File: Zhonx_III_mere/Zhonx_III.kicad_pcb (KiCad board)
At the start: 2 copper layers, 70 x 97 mm, 133 parts, among them K1 L_Motor, K2 R_Motor, K3 USART, P1 JTAG, Q1 FDV301N, Q2 FDV301N, U1 MCP73213, U10 BSL214N, U11 BSL214N, U12 24LC64T, U14 STM32F405RGT6, U16 Line_1, U17 Line_2, U18 Line_3, U19 Line_4, U2 A3918, U20 Line_5, U3 A3918, U4 LTC2955CTS8-2, U5 SIB911DK, U6 SI1551DL, U7 LM2940, U8 MCP1700, U9 MCP1700, X1 16MHz

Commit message: Update Base_V2 (CamBam DXF)
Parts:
- ADXR1, C103, C104, C17, C18, C19, C2, C20, C21, C22, C23, C24, C25, C27, C29, C30, C35, C36, C37, C38, C39, C40, C41, C43, D1, D11, D12, IR1, IR2, IR3, IR4, K1, K2, K3, L2, PL1, R1, R17, R18, R19, R22, R23, R3, R30, R34, R35, R38, R39, R44, R45, R48, R49, R50, R51, R52, SP1, U10, U11, U14, X1: moved to B.Cu
- C1, C10, C100, C101, C11, C12, C13, C14, C15, C16, C26, C28, C3, C31, C32, C33, C34, C4, C42, C44, C45, C5, C6, C7, C8, C9, P1, Q1, Q2, R10, R11, R12, R13, R14, R15, R16, R2, R20, R21, R24, R25, R26, R27, R28, R29, R31, R32, R33, R4, R5, R58, R6, R64, R67, R7, R8, R9, SCH1, U1, U12, U16, U17, U18, U19, U2, U20, U3, U4, U5, U6, U7, U8, U9: moved to F.Cu
- moved Q1 87.4 mm to (154.2, 125.6), turned to 180 degrees
- moved R8 86.5 mm to (153.7, 128.2), turned to 0 degrees
- moved C2 83.9 mm to (152.3, 129.2)
- moved C19 81.8 mm to (151.2, 129.2)
- moved R10 80.9 mm to (150.7, 129.7)
- moved IR1 79.1 mm to (149.7, 117.8), turned to 174 degrees
- moved R34 79.0 mm to (149.7, 128.8)
- moved C33 78.8 mm to (149.5, 129.7)
- moved R44 78.4 mm to (149.3, 120.9), turned to 0 degrees
- moved R35 77.4 mm to (148.8, 126.0), turned to 0 degrees
- moved D11 76.5 mm to (148.3, 186.0)
- moved R1 76.5 mm to (148.3, 183.5)
- moved R45 75.4 mm to (147.7, 120.9), turned to 0 degrees
- moved U10 73.4 mm to (146.6, 128.7)
- moved R18 72.5 mm to (146.0, 126.7), turned to 0 degrees
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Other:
- outline, holes or cut-outs redrawn

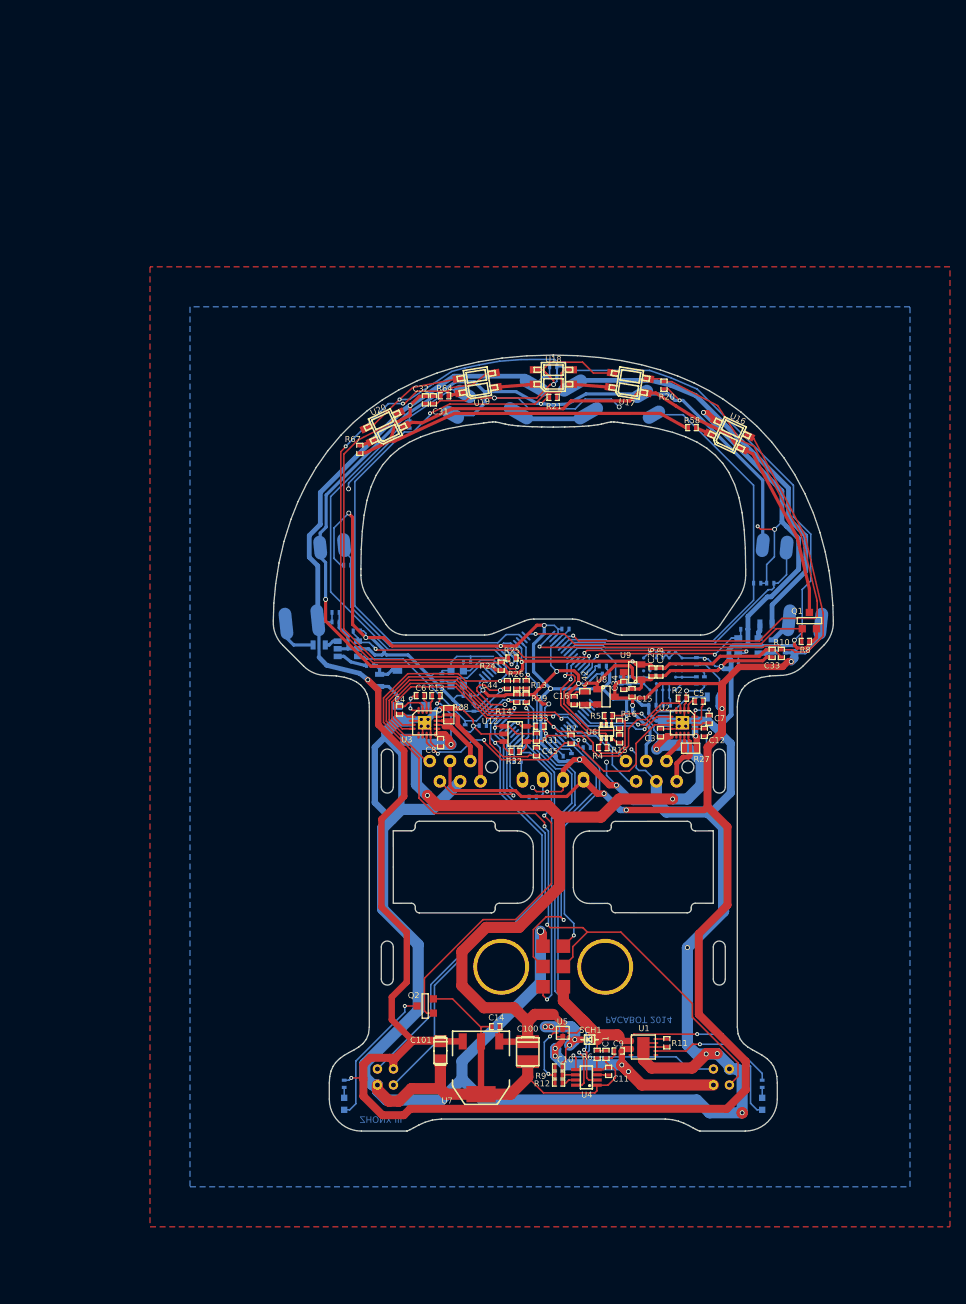
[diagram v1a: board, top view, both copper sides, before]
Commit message: repair mod librairies
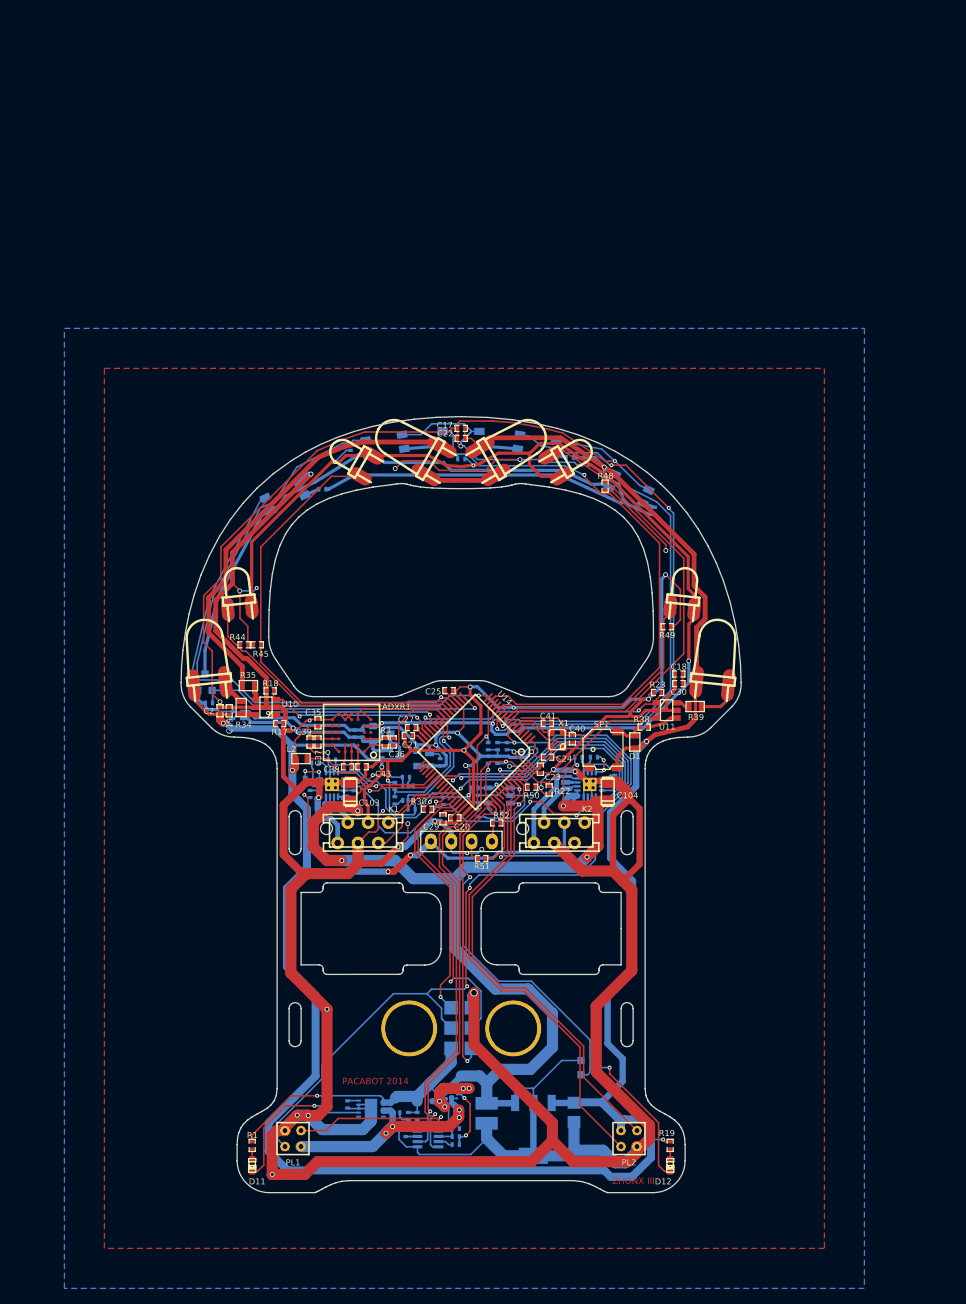
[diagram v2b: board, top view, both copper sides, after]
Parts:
- ADXR1, C103, C104, C17, C18, C19, C2, C20, C21, C22, C23, C24, C25, C27, C29, C30, C35, C36, C37, C38, C39, C40, C41, C43, D1, D11, D12, IR1, IR2, IR3, IR4, K1, K2, K3, L2, PL1, R1, R17, R18, R19, R22, R23, R3, R30, R34, R35, R38, R39, R44, R45, R48, R49, R50, R51, R52, SP1, U10, U11, U14, X1: moved to F.Cu
- C1, C10, C100, C101, C11, C12, C13, C14, C15, C16, C26, C28, C3, C31, C32, C33, C34, C4, C42, C44, C45, C5, C6, C7, C8, C9, P1, Q1, Q2, R10, R11, R12, R13, R14, R15, R16, R2, R20, R21, R24, R25, R26, R27, R28, R29, R31, R32, R33, R4, R5, R58, R6, R64, R67, R7, R8, R9, SCH1, U1, U12, U16, U17, U18, U19, U2, U20, U3, U4, U5, U6, U7, U8, U9: moved to B.Cu
- moved Q1 75.9 mm to (78.6, 133.3), turned to 0 degrees
- moved R8 74.9 mm to (79.1, 135.9), turned to 180 degrees
- moved C2 72.2 mm to (80.5, 136.8)
- moved C19 69.9 mm to (81.7, 136.8)
- moved R10 69.0 mm to (82.1, 137.4)
- moved IR1 67.0 mm to (83.1, 125.5), turned to 6 degrees
- moved R34 66.9 mm to (83.2, 136.4)
- moved C33 66.7 mm to (83.3, 137.4)
- moved R44 66.2 mm to (83.5, 128.6), turned to 180 degrees
- moved R35 65.2 mm to (84.0, 133.7), turned to 180 degrees
- moved D11 64.2 mm to (84.5, 193.7)
- moved R1 64.2 mm to (84.5, 191.2)
- moved R45 63.0 mm to (85.2, 128.6), turned to 180 degrees
- moved U10 60.8 mm to (86.2, 136.4)
- moved R18 59.8 mm to (86.8, 134.4), turned to 180 degrees
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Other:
- outline, holes or cut-outs redrawn
